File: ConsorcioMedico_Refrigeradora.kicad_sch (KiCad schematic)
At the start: 46 parts, among them J1 BatteryHolder, J37 SWD, J5 AC, J5 USART, J6 Screw_Terminal_01x01, J7 Screw_Terminal_01x01, J8 AC, U1 STM32F411RETx, U2 AP63205WU, U3 LDL1117, U9 HLK-PMx

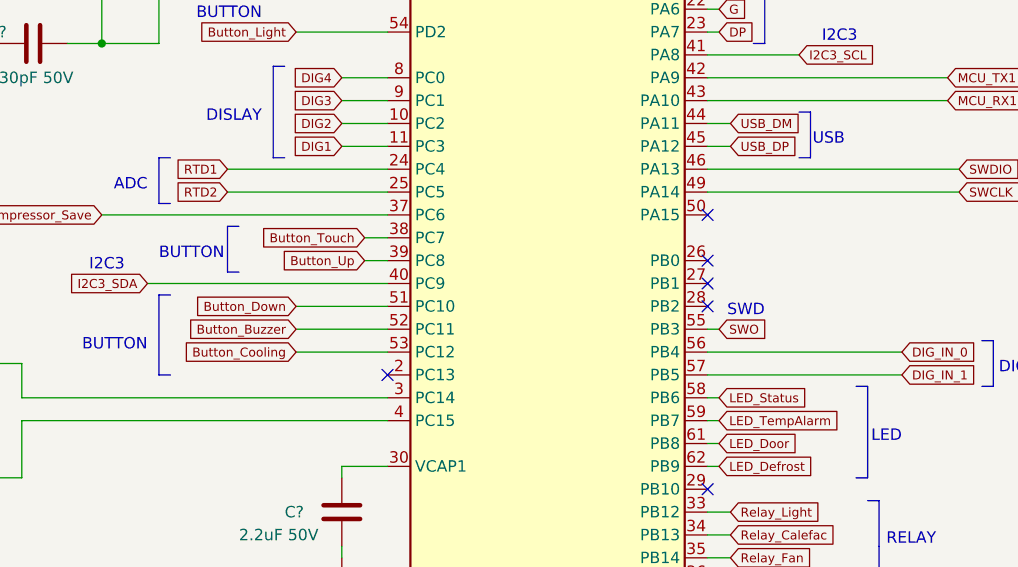
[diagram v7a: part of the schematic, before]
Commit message: SCH: Se arregló la posición de los pulsadores, se agrega buzzer, PCB: Se revisan los componentes y se agrega serigrafía. JLCPCB: Actualizado
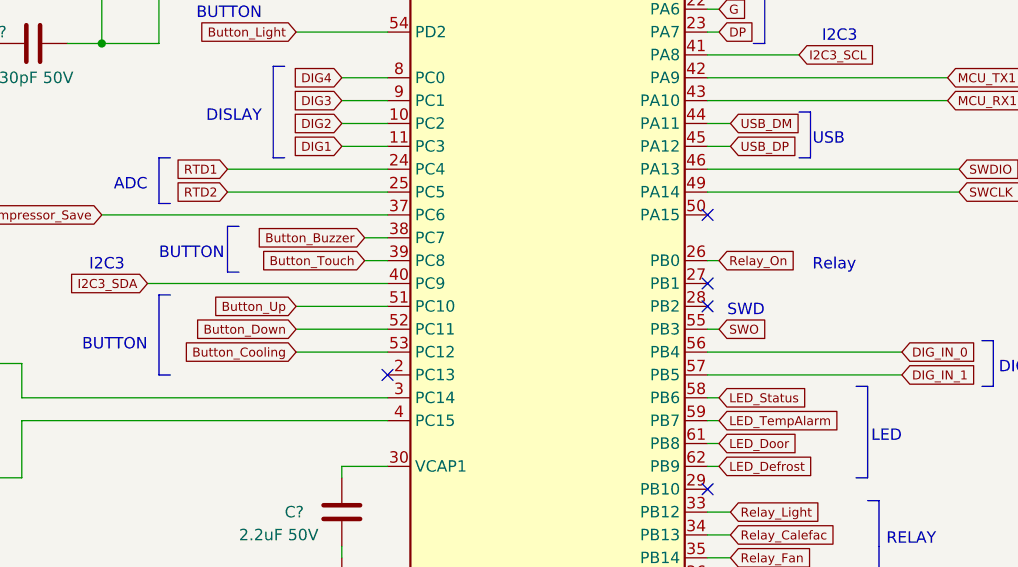
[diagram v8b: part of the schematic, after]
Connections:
- net Button_Buzzer: now also U1.38 (PC7); no longer U1.52 (PC11)
- net Button_Down: now also U1.52 (PC11); no longer U1.51 (PC10)
- net Button_Touch: now also U1.39 (PC8); no longer U1.38 (PC7)
- net Button_Up: now also U1.51 (PC10); no longer U1.39 (PC8)
- net Relay_On: now reaches U1.26 (PB0)
- no-connect marks 6 -> 5
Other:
- note added: "Relay"
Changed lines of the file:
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@@
   )
   (no_connect (at 412.75 109.22))
-  (no_connect (at 412.75 106.68))
   (no_connect (at 412.75 132.08))
   (no_connect (at 377.19 119.38))
@@
     (stroke (width 0) (type default))
   )
+  (wire (pts (xy 414.02 106.68) (xy 412.75 106.68))
+    (stroke (width 0) (type default))
+  )
   (wire (pts (xy 365.76 237.49) (xy 375.92 237.49))
     (stroke (width 0) (type default))
@@
     (effects (font (size 1.27 1.27)) (justify right bottom))
   )
+  (text "Relay" (at 429.26 107.95 0)
+    (effects (font (size 1.27 1.27)) (justify right bottom))
+  )
   (text "JTAG/SWD" (at 407.67 208.28 0)
     (effects (font (size 2 2)) (justify left bottom))
@@
     )
   )
+  (global_label "Button_Touch" (shape input) (at 374.65 106.68 180) (fields_autoplaced)
+    (effects (font (size 1 1)) (justify right))
+    (property "Intersheetrefs" "${INTERSHEET_REFS}" (at 362.4096 106.68 0)
+      (effects (font (size 1.27 1.27)) (justify right) hide)
+    )
+  )
   (global_label "MCU_TX1" (shape input) (at 439.42 86.36 0) (fields_autoplaced)
     (effects (font (size 1 1)) (justify left))
@@
     )
   )
-  (global_label "Button_Down" (shape input) (at 367.03 111.76 180) (fields_autoplaced)
-    (effects (font (size 1 1)) (justify right))
-    (property "Intersheetrefs" "${INTERSHEET_REFS}" (at 355.2658 111.76 0)
-      (effects (font (size 1.27 1.27)) (justify right) hide)
-    )
-  )
   (global_label "Relay_Fan" (shape input) (at 415.29 139.7 0) (fields_autoplaced)
     (effects (font (size 1 1)) (justify left))
@@
     )
   )
+  (global_label "Button_Down" (shape input) (at 367.03 114.3 180) (fields_autoplaced)
+    (effects (font (size 1 1)) (justify right))
+    (property "Intersheetrefs" "${INTERSHEET_REFS}" (at 355.2658 114.3 0)
+      (effects (font (size 1.27 1.27)) (justify right) hide)
+    )
+  )
   (global_label "G" (shape input) (at 414.02 78.74 0) (fields_autoplaced)
     (effects (font (size 1 1)) (justify left))
@@
     )
   )
-  (global_label "Button_Touch" (shape input) (at 374.65 104.14 180) (fields_autoplaced)
-    (effects (font (size 1 1)) (justify right))
-    (property "Intersheetrefs" "${INTERSHEET_REFS}" (at 362.4096 104.14 0)
-      (effects (font (size 1.27 1.27)) (justify right) hide)
+  (global_label "Relay_On" (shape input) (at 414.02 106.68 0) (fields_autoplaced)
+    (effects (font (size 1 1)) (justify left))
+    (property "Intersheetrefs" "${INTERSHEET_REFS}" (at 423.0698 106.68 0)
+      (effects (font (size 1.27 1.27)) (justify left) hide)
     )
   )
@@
     )
   )
+  (global_label "Button_Buzzer" (shape input) (at 374.65 104.14 180) (fields_autoplaced)
+    (effects (font (size 1 1)) (justify right))
+    (property "Intersheetrefs" "${INTERSHEET_REFS}" (at 361.7431 104.14 0)
+      (effects (font (size 1.27 1.27)) (justify right) hide)
+    )
+  )
   (global_label "I2C3_SDA" (shape input) (at 350.52 109.22 180) (fields_autoplaced)
     (effects (font (size 1 1)) (justify right))
@@
     )
   )
-  (global_label "Button_Buzzer" (shape input) (at 367.03 114.3 180) (fields_autoplaced)
-    (effects (font (size 1 1)) (justify right))
-    (property "Intersheetrefs" "${INTERSHEET_REFS}" (at 354.1231 114.3 0)
-      (effects (font (size 1.27 1.27)) (justify right) hide)
-    )
-  )
   (global_label "D" (shape input) (at 414.02 71.12 0) (fields_autoplaced)
     (effects (font (size 1 1)) (justify left))
@@
     )
   )
-  (global_label "Button_Up" (shape input) (at 374.65 106.68 180) (fields_autoplaced)
-    (effects (font (size 1 1)) (justify right))
-    (property "Intersheetrefs" "${INTERSHEET_REFS}" (at 364.7906 106.68 0)
-      (effects (font (size 1.27 1.27)) (justify right) hide)
-    )
-  )
   (global_label "LED_Status" (shape input) (at 414.02 121.92 0) (fields_autoplaced)
     (effects (font (size 1 1)) (justify left))
@@
     )
   )
+  (global_label "Button_Up" (shape input) (at 367.03 111.76 180) (fields_autoplaced)
+    (effects (font (size 1 1)) (justify right))
+    (property "Intersheetrefs" "${INTERSHEET_REFS}" (at 357.1706 111.76 0)
+      (effects (font (size 1.27 1.27)) (justify right) hide)
+    )
+  )
